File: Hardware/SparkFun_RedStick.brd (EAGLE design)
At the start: 17.8 x 66 mm, 42 parts, among them Q1 DMG2307L, Q2 MOSFET-NCHANNEL2N7002PW, U1 FTS31XS-U, U2 ATMEGA328P_TQFP, U4 5.0v, Y1 16MHZ

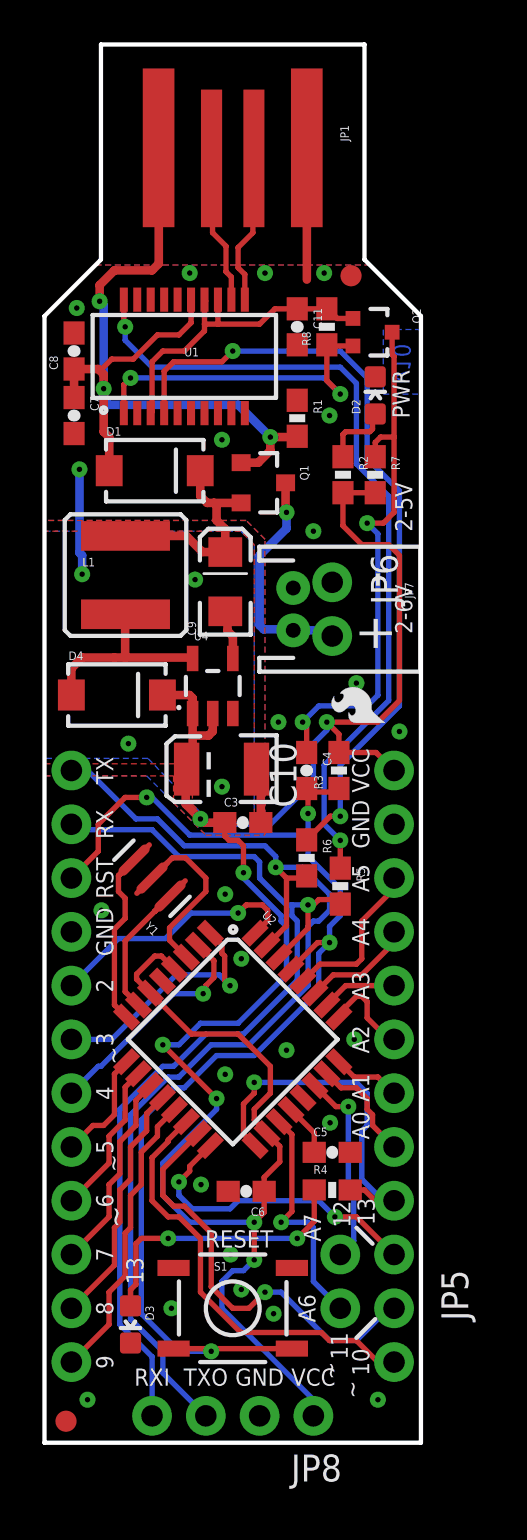
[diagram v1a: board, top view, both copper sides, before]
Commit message: Re-approved DRC, renamed U4
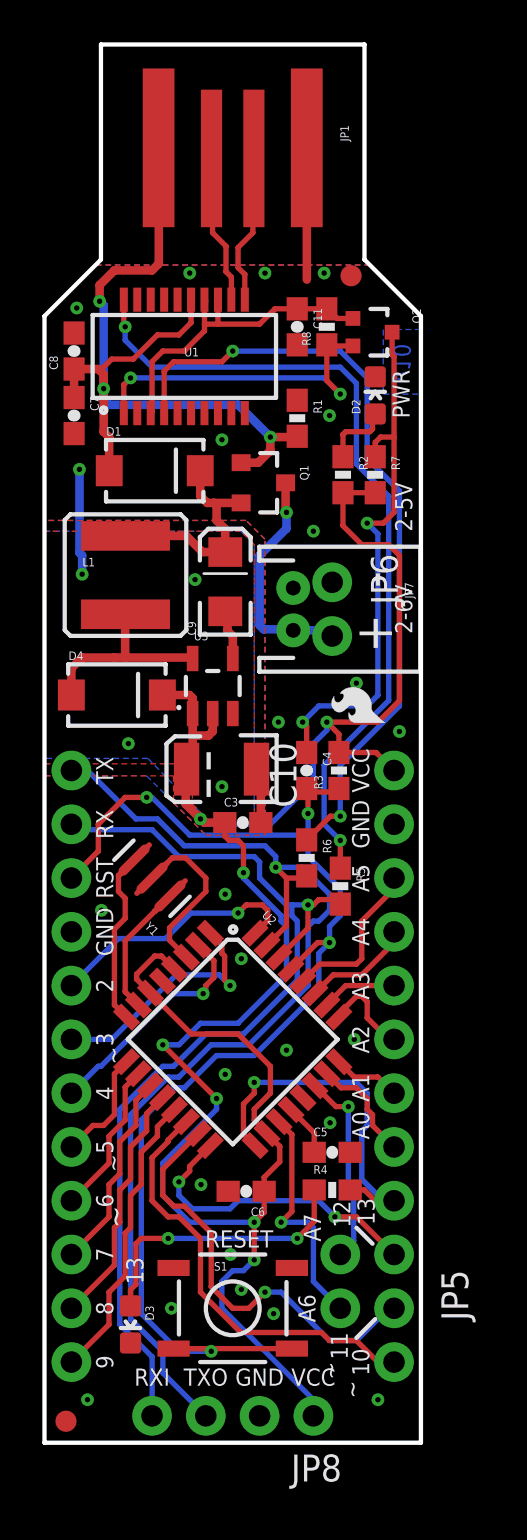
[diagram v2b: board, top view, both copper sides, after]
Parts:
- renumbered U4 to U3
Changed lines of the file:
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@@
 <layer number="20" name="Dimension" color="15" fill="1" visible="yes" active="yes"/>
 <layer number="21" name="tPlace" color="16" fill="1" visible="no" active="yes"/>
-<layer number="22" name="bPlace" color="14" fill="1" visible="yes" active="yes"/>
+<layer number="22" name="bPlace" color="14" fill="1" visible="no" active="yes"/>
 <layer number="23" name="tOrigins" color="15" fill="1" visible="no" active="yes"/>
-<layer number="24" name="bOrigins" color="15" fill="1" visible="no" active="yes"/>
+<layer number="24" name="bOrigins" color="15" fill="1" visible="yes" active="yes"/>
 <layer number="25" name="tNames" color="7" fill="1" visible="no" active="yes"/>
 <layer number="26" name="bNames" color="7" fill="1" visible="no" active="yes"/>
@@
 </class>
 </classes>
-<designrules name="SparkFun-2-layer-STANDARD">
+<designrules name="SparkFun-2-layer-TIGHT">
 <description language="en">&lt;b&gt;SparkFun 2 Layer Design Rule Checks - STANDARD/TIGHT/FAB-LIMIT&lt;/b&gt;
 &lt;p&gt;
@@
 <param name="mtCopper" value="0.035mm 0.035mm 0.035mm 0.035mm 0.035mm 0.035mm 0.035mm 0.035mm 0.035mm 0.035mm 0.035mm 0.035mm 0.035mm 0.035mm 0.035mm 0.035mm"/>
 <param name="mtIsolate" value="1.5mm 0.15mm 0.2mm 0.15mm 0.2mm 0.15mm 0.2mm 0.15mm 0.2mm 0.15mm 0.2mm 0.15mm 0.2mm 0.15mm 0.2mm"/>
-<param name="mdWireWire" value="10mil"/>
-<param name="mdWirePad" value="8mil"/>
-<param name="mdWireVia" value="10mil"/>
-<param name="mdPadPad" value="8mil"/>
-<param name="mdPadVia" value="10mil"/>
-<param name="mdViaVia" value="10mil"/>
-<param name="mdSmdPad" value="8mil"/>
-<param name="mdSmdVia" value="8mil"/>
-<param name="mdSmdSmd" value="8mil"/>
+<param name="mdWireWire" value="7mil"/>
+<param name="mdWirePad" value="7mil"/>
+<param name="mdWireVia" value="7mil"/>
+<param name="mdPadPad" value="7mil"/>
+<param name="mdPadVia" value="7mil"/>
+<param name="mdViaVia" value="7mil"/>
+<param name="mdSmdPad" value="7mil"/>
+<param name="mdSmdVia" value="7mil"/>
+<param name="mdSmdSmd" value="7mil"/>
 <param name="mdViaViaSameLayer" value="8mil"/>
 <param name="mnLayersViaInSmd" value="2"/>
-<param name="mdCopperDimension" value="8mil"/>
-<param name="mdDrill" value="8mil"/>
+<param name="mdCopperDimension" value="7mil"/>
+<param name="mdDrill" value="7mil"/>
 <param name="mdSmdStop" value="0mil"/>
-<param name="msWidth" value="10mil"/>
-<param name="msDrill" value="20mil"/>
+<param name="msWidth" value="7mil"/>
+<param name="msDrill" value="15mil"/>
 <param name="msMicroVia" value="9.99mm"/>
 <param name="msBlindViaRatio" value="0.5"/>
@@
 <param name="rvMicroViaOuter" value="0.25"/>
 <param name="rvMicroViaInner" value="0.25"/>
-<param name="rlMinPadTop" value="10mil"/>
+<param name="rlMinPadTop" value="7mil"/>
 <param name="rlMaxPadTop" value="20mil"/>
-<param name="rlMinPadInner" value="10mil"/>
+<param name="rlMinPadInner" value="7mil"/>
 <param name="rlMaxPadInner" value="20mil"/>
-<param name="rlMinPadBottom" value="10mil"/>
+<param name="rlMinPadBottom" value="7mil"/>
 <param name="rlMaxPadBottom" value="20mil"/>
-<param name="rlMinViaOuter" value="10mil"/>
+<param name="rlMinViaOuter" value="7mil"/>
 <param name="rlMaxViaOuter" value="20mil"/>
-<param name="rlMinViaInner" value="10mil"/>
+<param name="rlMinViaInner" value="7mil"/>
 <param name="rlMaxViaInner" value="20mil"/>
 <param name="rlMinMicroViaOuter" value="4mil"/>
@@
 <element name="JP3" library="SparkFun-Connectors" package="1X12_NO_SILK" value="DNP" x="16.51" y="31.75" rot="R270"/>
 <element name="FRAME2" library="SparkFun-Aesthetics" package="CREATIVE_COMMONS" value="FRAME-LEDGER" x="-20.0914" y="-29.3116"/>
-<element name="U4" library="SparkFun-PowerIC" package="SOT23-5" value="5.0v" x="7.947025" y="35.740975">
+<element name="U3" library="SparkFun-PowerIC" package="SOT23-5" value="5.0v" x="7.947025" y="35.740975">
 <attribute name="PROD_ID" value="IC-10787" x="7.947025" y="35.740975" size="1.778" layer="27" display="off"/>
 <attribute name="VALUE" value="5.0v" x="7.947025" y="35.740975" size="1.778" layer="27" display="off"/>
@@
 <contactref element="C3" pad="2"/>
 <contactref element="C10" pad="C"/>
-<contactref element="U4" pad="4"/>
+<contactref element="U3" pad="4"/>
 <contactref element="C9" pad="C"/>
 <wire x1="8.537575" y1="39.268575" x2="8.643025" y2="39.163125" width="0.4064" layer="1"/>
@@
 </signal>
 <signal name="N$8">
-<contactref element="U4" pad="5"/>
+<contactref element="U3" pad="5"/>
 <contactref element="D4" pad="A"/>
 <contactref element="L1" pad="P$2"/>
@@
 <contactref element="U2" pad="6"/>
 <contactref element="U2" pad="18"/>
-<contactref element="U4" pad="1"/>
-<contactref element="U4" pad="2"/>
+<contactref element="U3" pad="1"/>
+<contactref element="U3" pad="2"/>
 <contactref element="C10" pad="A"/>
 <contactref element="C3" pad="1"/>
@@
 </signal>
 </signals>
+<errors>
+</errors>
 </board>
 </drawing>
